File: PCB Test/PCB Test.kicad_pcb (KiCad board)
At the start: 2 copper layers, 51.6 x 67.2 mm, 50 parts, among them J1 Conn_02x02_Odd_Even, J2 Conn_02x05_Odd_Even, J3 Conn_02x02_Counter_Clockwise, J4 Conn_02x02_Counter_Clockwise, J5 Conn_02x02_Counter_Clockwise, J6 Conn_02x03_Odd_Even, Q2 NMOS, Q3 NMOS, SW1 SW_Push, SW2 SW_Push, SW3 SW_Push, U1 ATmega4808-A, U5 MCP1700x-330xxTO

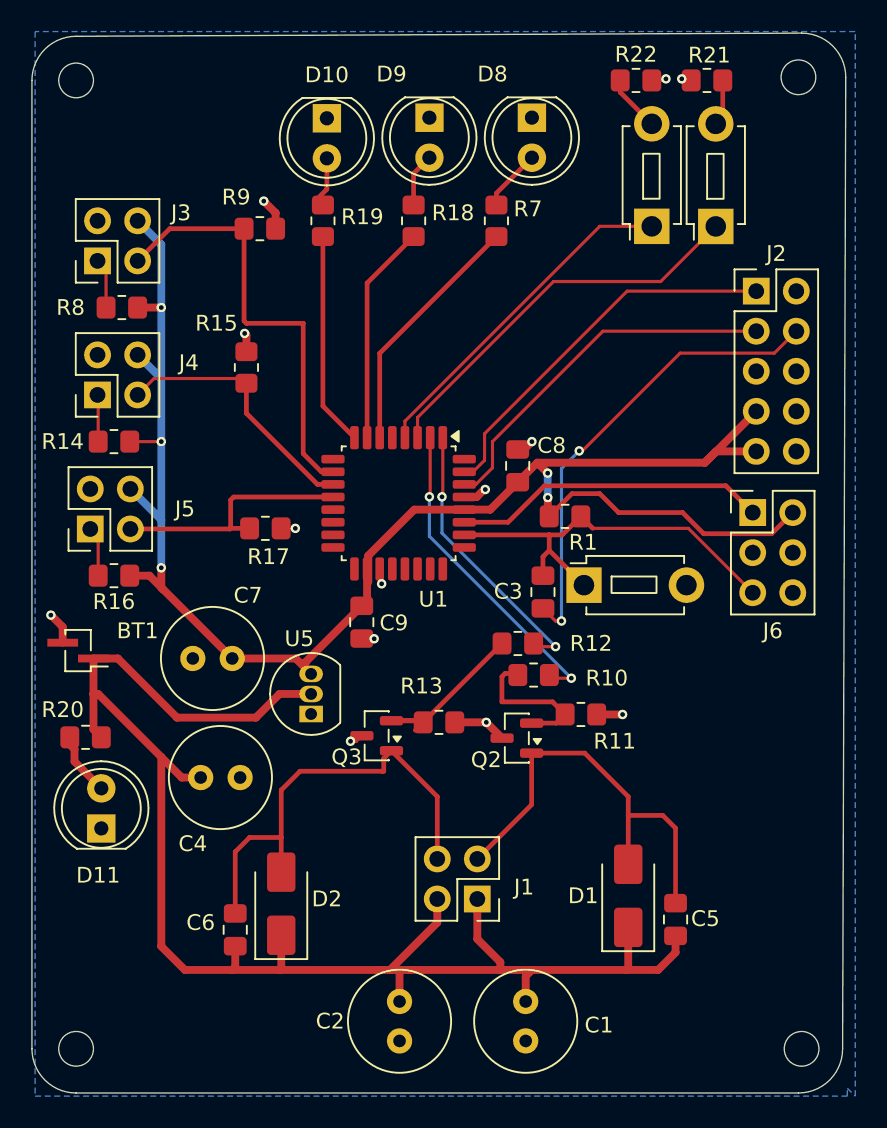
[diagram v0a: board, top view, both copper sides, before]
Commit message: Generated Gerber, Drill, updated buttons
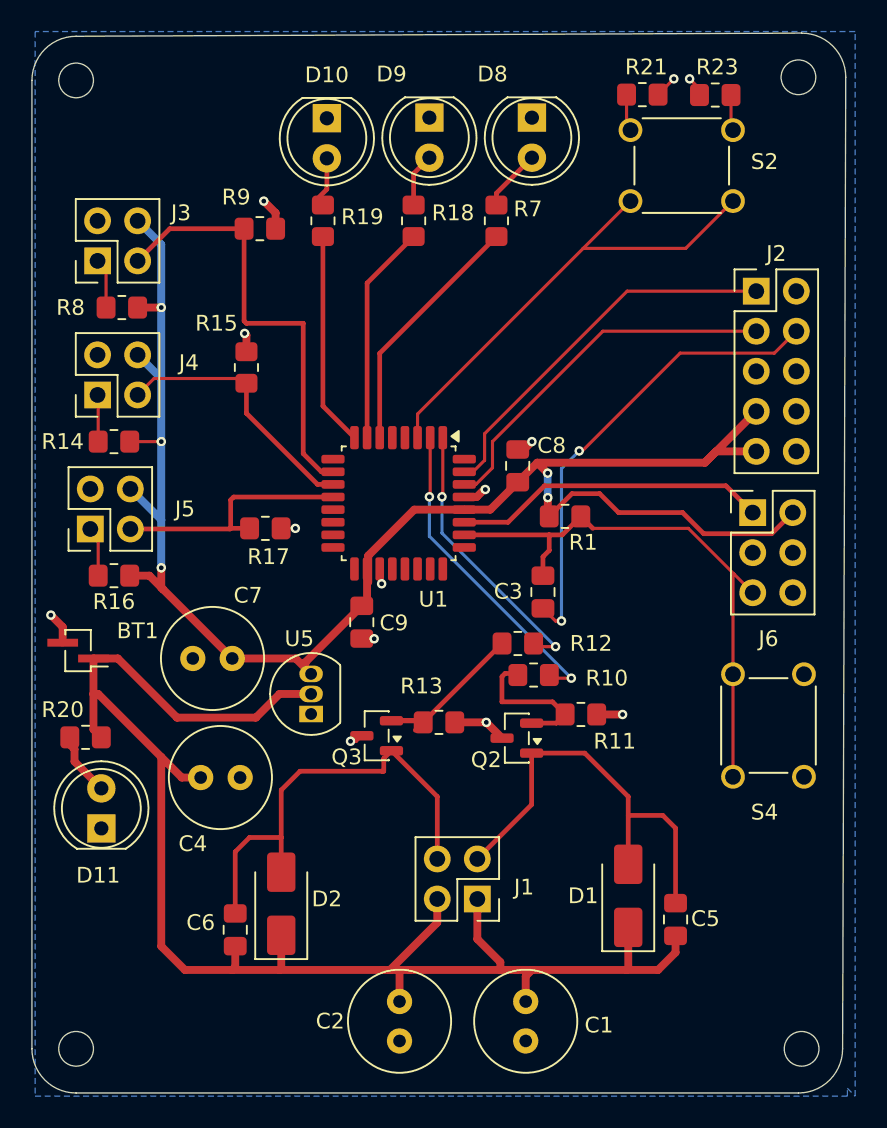
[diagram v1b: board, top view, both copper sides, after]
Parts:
- removed R22: 680, Resistor_SMD:R_0805_2012Metric_Pad1.20x1.40mm_HandSolder
- removed SW1, SW2, SW3: SW_Push, Button_Switch_THT:SW_PUSH_1P1T_6x3.5mm_H4.3_APEM_MJTP1243
- added R23: 680, Resistor_SMD:R_0805_2012Metric_Pad1.20x1.40mm_HandSolder, F.Cu at (176.1, 92.5)
- added S2: MJTP1230, MJTP1230:SW_MJTP1230, F.Cu at (174.0, 97.0)
- added S4: MJTP1230, MJTP1230:SW_MJTP1230, F.Cu at (179.5, 132.5)
- moved R21 4.20 mm to (171.5, 92.5), turned to 0 degrees
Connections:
- U1 pad 4: Button 2 -> unconnected-(U1-PA6-Pad4)
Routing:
- net Button 2: track 21.8 -> 0.00 mm
- net RESET: track 26.2 -> 36.0 mm
- net Button 1: track 25.2 -> 31.3 mm
- net Net-(R22-Pad1): track 3.58 -> 0.00 mm
- net Net-(R23-Pad1): track 0.00 -> 2.28 mm
- net GND: track 18.6 -> 19.7 mm
- net Net-(R21-Pad1): track 2.94 -> 2.35 mm
